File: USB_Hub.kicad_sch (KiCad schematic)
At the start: 44 parts, among them U4 VL822-QFN76, U5 AP7331-10WG-7, Y1 25MHz

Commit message: Updated schematics
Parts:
- added R24, R25, R26, R27: 100k, Resistor_SMD:R_0402_1005Metric, symbol Device:R
- C10, C11, C12, C13, C14, C16, C17, C27, C28, C29, C30, C31, C33, C34: value 100nF -> 0.1µF; LCSC C60474 -> C307331; Part_Number CC0402KRX7R7BB104 -> CL05B104KB54PNC
- C15, C19, C32: LCSC C77019 -> C15195; Part_Number GRM155R71H103KA88D -> CL05B103KB5NNNC
- C35: LCSC C59782 -> C15849; Part_Number CL10B105KO8NNNC -> CL10A105KB8NNNC
- C36: footprint (none) -> Capacitor_SMD:C_0603_1608Metric; LCSC C8032 -> C19666; Part_Number CL10A475KQ8NNNC -> CL10A475KO8NNNC
- C65, C66, C67, C68, C69, C70, C71, C72, C73, C74: footprint Capacitor_SMD:C_0201_0603Metric -> Capacitor_SMD:C_0402_1005Metric; LCSC C160831 -> C307331; Part_Number CL03A104KQ3NNNC -> CL05B104KB54PNC
- R17, R18, R19, R20: LCSC C105870 -> C25900; Part_Number RC0402JR-074K7L -> 0402WGF4701TCE
- R2, R22, R23, R7, R8: LCSC C60490 -> C25744; Part_Number RC0402FR-0710KL -> 0402WGF1002TCE
- R21: footprint Resistor_SMD:R_0603_1608Metric -> Resistor_SMD:R_0805_2012Metric_Pad1.20x1.40mm_HandSolder; LCSC C728611 -> C966572; Part_Number RT0603DRD0712K4L -> CQ05W8F1242T5E
- U4: footprint kicad_lceda:QFN-76_L9.0-W9.0-P0.40-EP6.3-TL -> VL822-QFN76:VL822-QFN76
- U5: footprint kicad_lceda:SOT-25_L3.0-W1.6-P0.95-LS2.8-BL -> AP7331-10WG-7:AP7331-10WG-7
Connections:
- net +3V3: now also R24.2, R25.2, R26.1, R27.1
- net SSTX3+: now reaches C69.2, U4.25 (SSTX3+)
- net SSTX4+: now reaches C71.2, U4.31 (SSTX4+)
- net SSTX2+: now reaches C67.2, U4.12 (SSTX2+)
- net SSTX2-: now reaches C68.2, U4.13 (SSTX2–)
- net USB_DFP0_EN: now reaches U4.2 (USBPE1)
- net USB_DFP0_EN: now also R24.1
- net USB_DFP2_EN: now reaches U4.21 (USBPE3)
- net USB_DFP2_EN: now also R26.2
- net SSTX3-: now reaches C70.2, U4.26 (SSTX3–)
- net SSTX1+: now reaches C65.2, U4.3 (SSTX1+)
- net SSTX4-: now reaches C72.2, U4.32 (SSTX4–)
- net USB_DFP3_EN: now reaches U4.39 (USBPE4)
- net USB_DFP3_EN: now also R27.2
- net SSTX1-: now reaches C66.2, U4.4 (SSTX1–)
- net SSTX0-: now reaches C74.1, U4.49 (SSTX0–)
- net SSTX0+: now reaches C73.1, U4.50 (SSTX0+)
- net USB_DFP1_EN: now reaches U4.76 (USBPE2)
- net USB_DFP1_EN: now also R25.1
- net USBOC1 renamed USB_DFP0_FLT
- net USBOC2 renamed USB_DFP1_FLT
- net USBOC3 renamed USB_DFP2_FLT
- net USBOC4 renamed USB_DFP3_FLT
- net USB_DFP0_DM renamed USB_DFP0_DN
- net USB_DFP1_DM renamed USB_DFP1_DN
- net USB_DFP2_DM renamed USB_DFP2_DN
- net USB_DFP3_DM renamed USB_DFP3_DN
- net USB_UFP_DM renamed USB_UFP_DN
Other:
- note added: "VBUS Enables"
- note added: "VBUS OC Input"
- note removed: "Disable USB Overcurrent Protection"
- moved on the sheet: R2, R22, R23, R7, R8

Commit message: Continue working on board layout
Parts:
- added R75: 4.7k, Resistor_SMD:R_0402_1005Metric, symbol Device:R
- added R76: 10k, Resistor_SMD:R_0402_1005Metric, symbol Device:R
- added R77: 2M, Resistor_SMD:R_0603_1608Metric, symbol Device:R
- Y1: symbol Device:Crystal -> Device:Crystal_GND24; LCSC C2962753 -> C9006; Part_Number XC32M4-25.000-F20LJDTL -> X322525MOB4SI
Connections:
- net GND: now also Y1.2, Y1.4, R76.2
- net VBUSDET: now also R77.2
- net XO: now also Y1.3; no longer Y1.2
- new net: R75.2, R76.1, R77.1
- new net +5V: R75.1
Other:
- note added: "VBUS Detect"

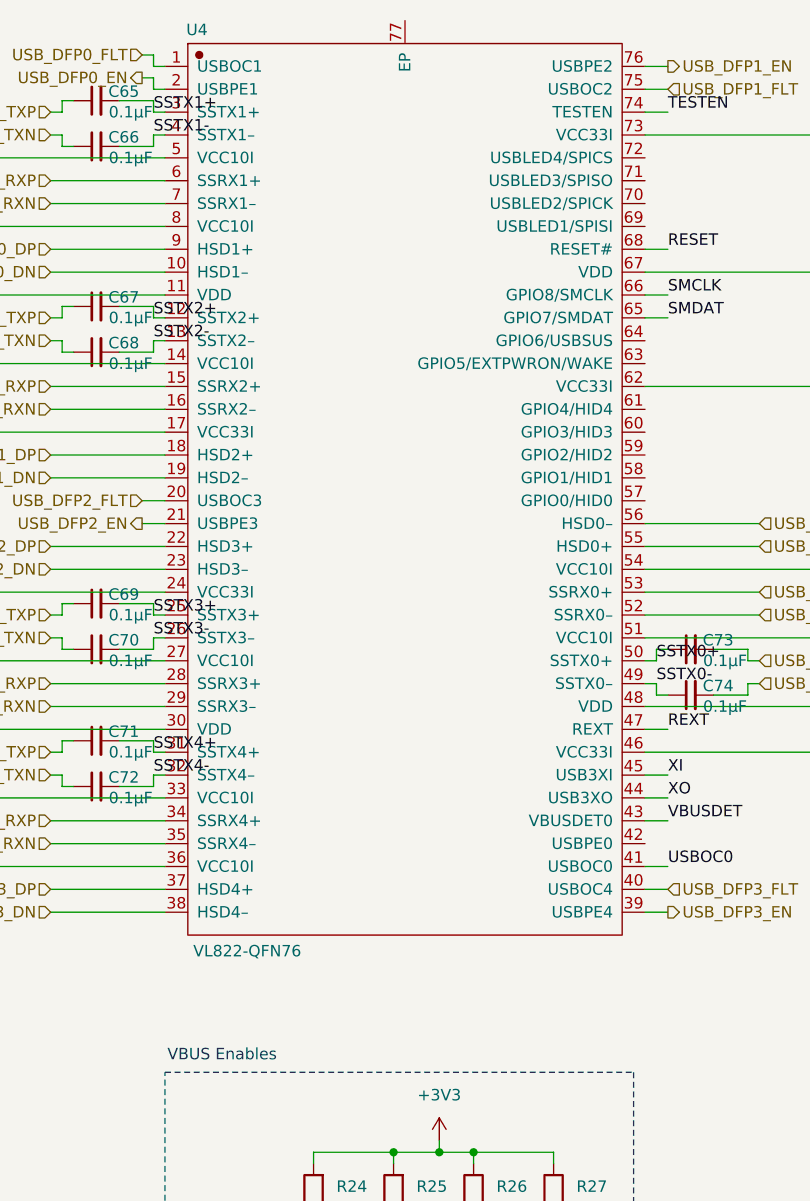
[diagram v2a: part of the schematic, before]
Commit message: Lay out more components
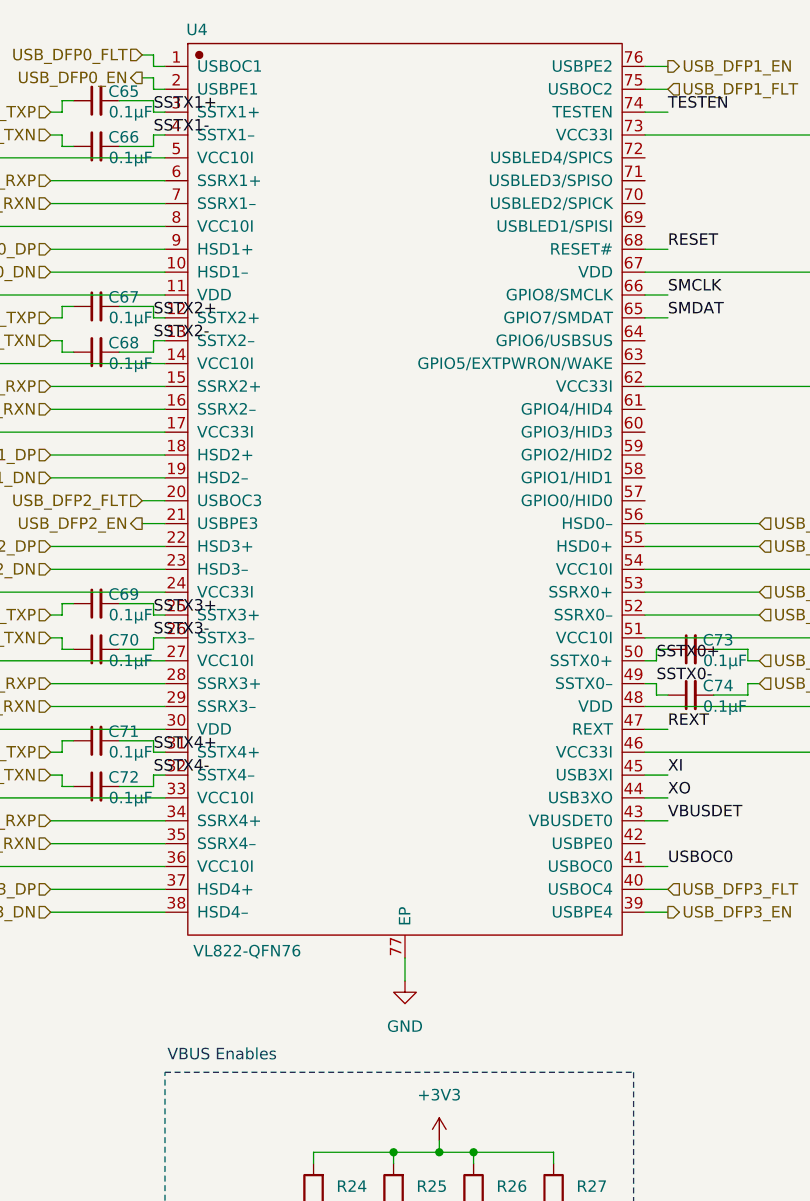
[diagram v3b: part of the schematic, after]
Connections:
- net GND: now also U4.77 (EP)
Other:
- moved on the sheet: U4
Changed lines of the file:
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@@
 	(wire
 		(pts
+			(xy 148.59 119.38) (xy 148.59 121.92)
+		)
+		(stroke
+			(width 0)
+			(type default)
+		)
+	)
+	(wire
+		(pts
 			(xy 20.32 110.49) (xy 20.32 115.57)
 		)
@@
 					(unit 1)
 				)
+			)
+		)
+	)
+	(symbol
+		(lib_id "power:GND")
+		(at 148.59 121.92 0)
+		(unit 1)
+		(exclude_from_sim no)
+		(in_bom yes)
+		(on_board yes)
+		(dnp no)
+		(fields_autoplaced yes)
+		(property "Reference" "#PWR0103"
+			(at 148.59 128.27 0)
+			(effects
+				(font
+					(size 1.27 1.27)
+				)
+				(hide yes)
+			)
+		)
+		(property "Value" "GND"
+			(at 148.59 127 0)
+			(effects
+				(font
+					(size 1.27 1.27)
+				)
+			)
+		)
+		(property "Footprint" ""
+			(at 148.59 121.92 0)
+			(effects
+				(font
+					(size 1.27 1.27)
+				)
+				(hide yes)
+			)
+		)
+		(property "Datasheet" ""
+			(at 148.59 121.92 0)
+			(effects
+				(font
+					(size 1.27 1.27)
+				)
+				(hide yes)
+			)
+		)
+		(property "Description" "Power symbol creates a global label with name \"GND\" , ground"
+			(at 148.59 121.92 0)
+			(effects
+				(font
+					(size 1.27 1.27)
+				)
+				(hide yes)
+			)
+		)
+		(pin "1"
+		)
+		(instances
+			(project "XG_Mobile_Dock"
+				(path "/f97e6956-ab08-42cb-8fed-03fa58e87f0e/ef21a87f-222f-4a81-a291-59975487be1d"
+					(reference "#PWR0103")
+					(unit 1)
+				)

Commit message: Updated board layout
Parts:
- C91, C92: LCSC C376770 -> C1653; Part_Number TCC0603COG180J500CT -> CL10C220JB8NNNC
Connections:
- net GND: now also U5.2 (GND)
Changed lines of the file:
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@@
 	)
 	(junction
+		(at 26.67 182.88)
+		(diameter 0)
+		(color 0 0 0 0)
+	)
+	(junction
 		(at 20.32 120.65)
 		(diameter 0)
@@
 	(wire
 		(pts
+			(xy 26.67 182.88) (xy 26.67 185.42)
+		)
+		(stroke
+			(width 0)
+			(type default)
+		)
+	)
+	(wire
+		(pts
 			(xy 245.11 93.98) (xy 245.11 102.87)
 		)
@@
 	(wire
 		(pts
+			(xy 35.56 182.88) (xy 26.67 182.88)
+		)
+		(stroke
+			(width 0)
+			(type default)
+		)
+	)
+	(wire
+		(pts
 			(xy 74.93 78.74) (xy 121.92 78.74)
 		)
@@
 	(wire
 		(pts
-			(xy 26.67 181.61) (xy 26.67 185.42)
+			(xy 26.67 181.61) (xy 26.67 182.88)
 		)
 		(stroke
@@
 	(wire
 		(pts
+			(xy 38.1 177.8) (xy 35.56 177.8)
+		)
+		(stroke
+			(width 0)
+			(type default)
+		)
+	)
+	(wire
+		(pts
 			(xy 20.32 120.65) (xy 64.77 120.65)
 		)
@@
 	(wire
 		(pts
+			(xy 35.56 177.8) (xy 35.56 182.88)
+		)
+		(stroke
+			(width 0)
+			(type default)
+		)
+	)
+	(wire
+		(pts
 			(xy 175.26 88.9) (xy 176.53 88.9)
 		)
@@
 			)
 		)
-		(property "LCSC" "C376770"
+		(property "LCSC" "C1653"
 			(at 256.54 123.19 0)
 			(effects
@@
 			)
 		)
-		(property "Part_Number" "TCC0603COG180J500CT"
+		(property "Part_Number" "CL10C220JB8NNNC"
 			(at 256.54 123.19 0)
 			(effects
@@
 			)
 		)
-		(property "LCSC" "C376770"
+		(property "LCSC" "C1653"
 			(at 266.7 123.19 0)
 			(effects
@@
 			)
 		)
-		(property "Part_Number" "TCC0603COG180J500CT"
+		(property "Part_Number" "CL10C220JB8NNNC"
 			(at 266.7 123.19 0)
 			(effects

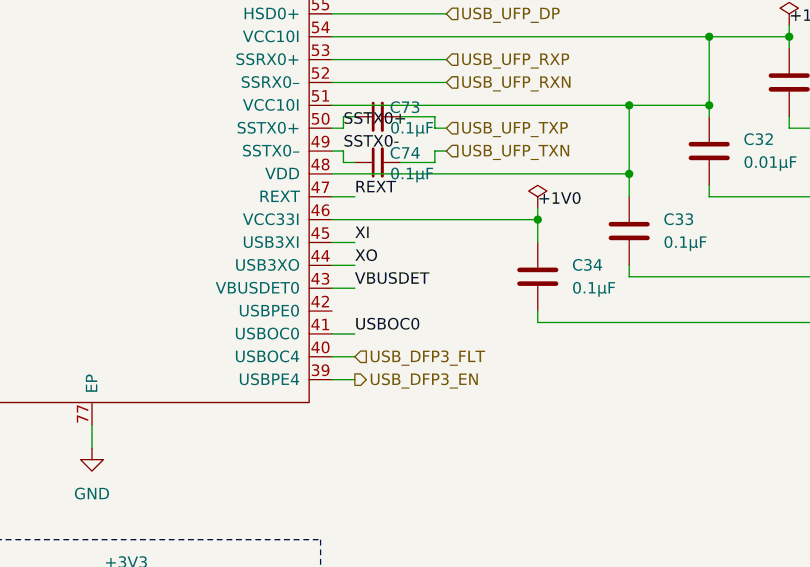
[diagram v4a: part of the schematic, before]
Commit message: Add TPS65987D charger circuit
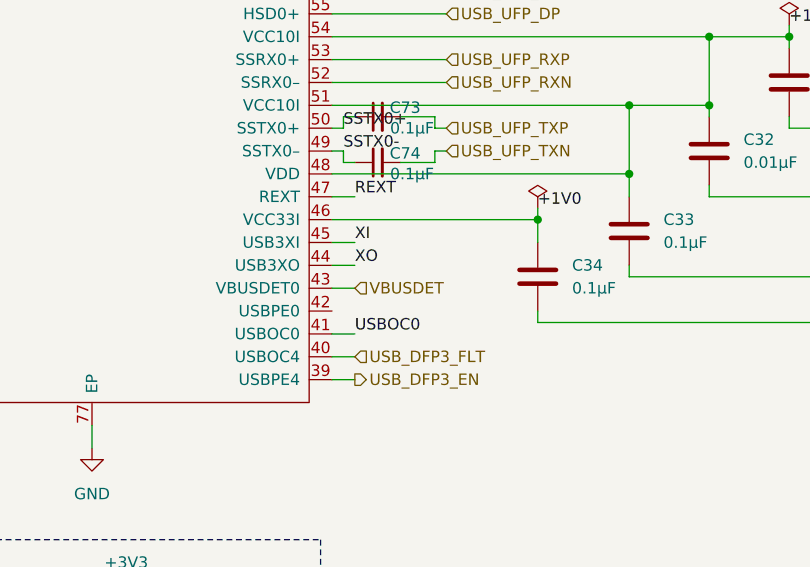
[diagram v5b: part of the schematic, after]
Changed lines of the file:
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@@
-		)
-	)
-	(label "VBUSDET"
-		(at 177.8 104.14 0)
-		(fields_autoplaced yes)
-		(effects
-			(font
-				(size 1.27 1.27)
-			)
-			(justify left bottom)
 		)
 	)
@@
 		)
 	)
+	(hierarchical_label "VBUSDET"
+		(shape input)
+		(at 177.8 104.14 0)
+		(fields_autoplaced yes)
+		(effects
+			(font
+				(size 1.27 1.27)
+			)
+			(justify left)
+		)
+	)

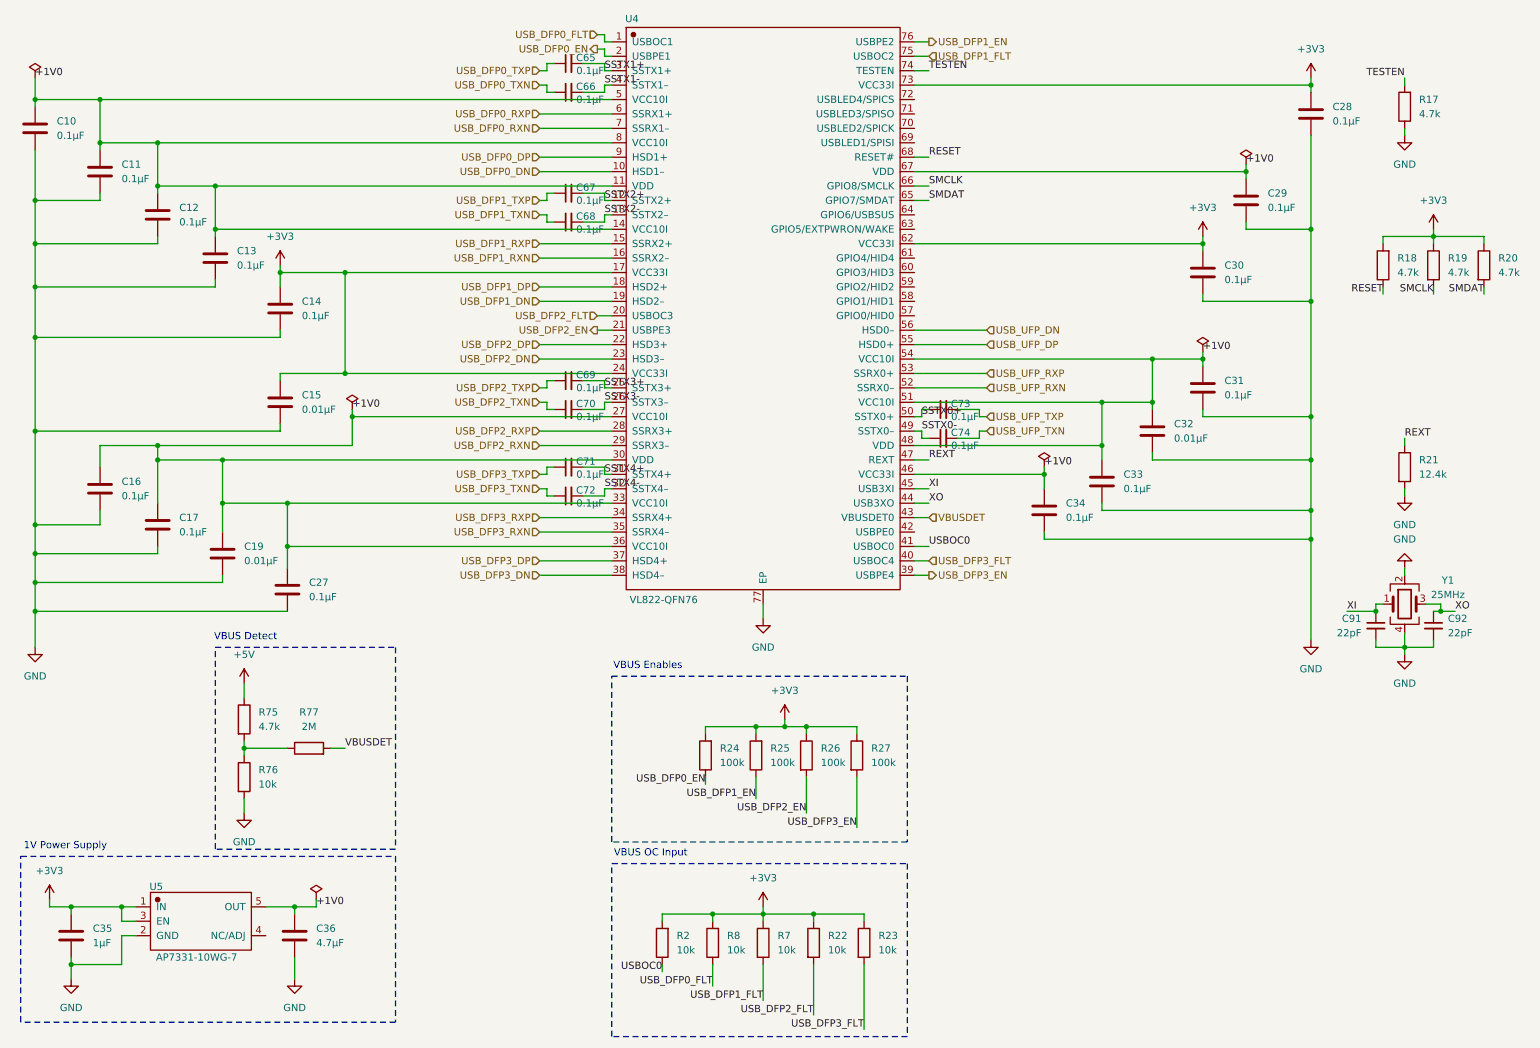
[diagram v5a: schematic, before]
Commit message: Added MCU
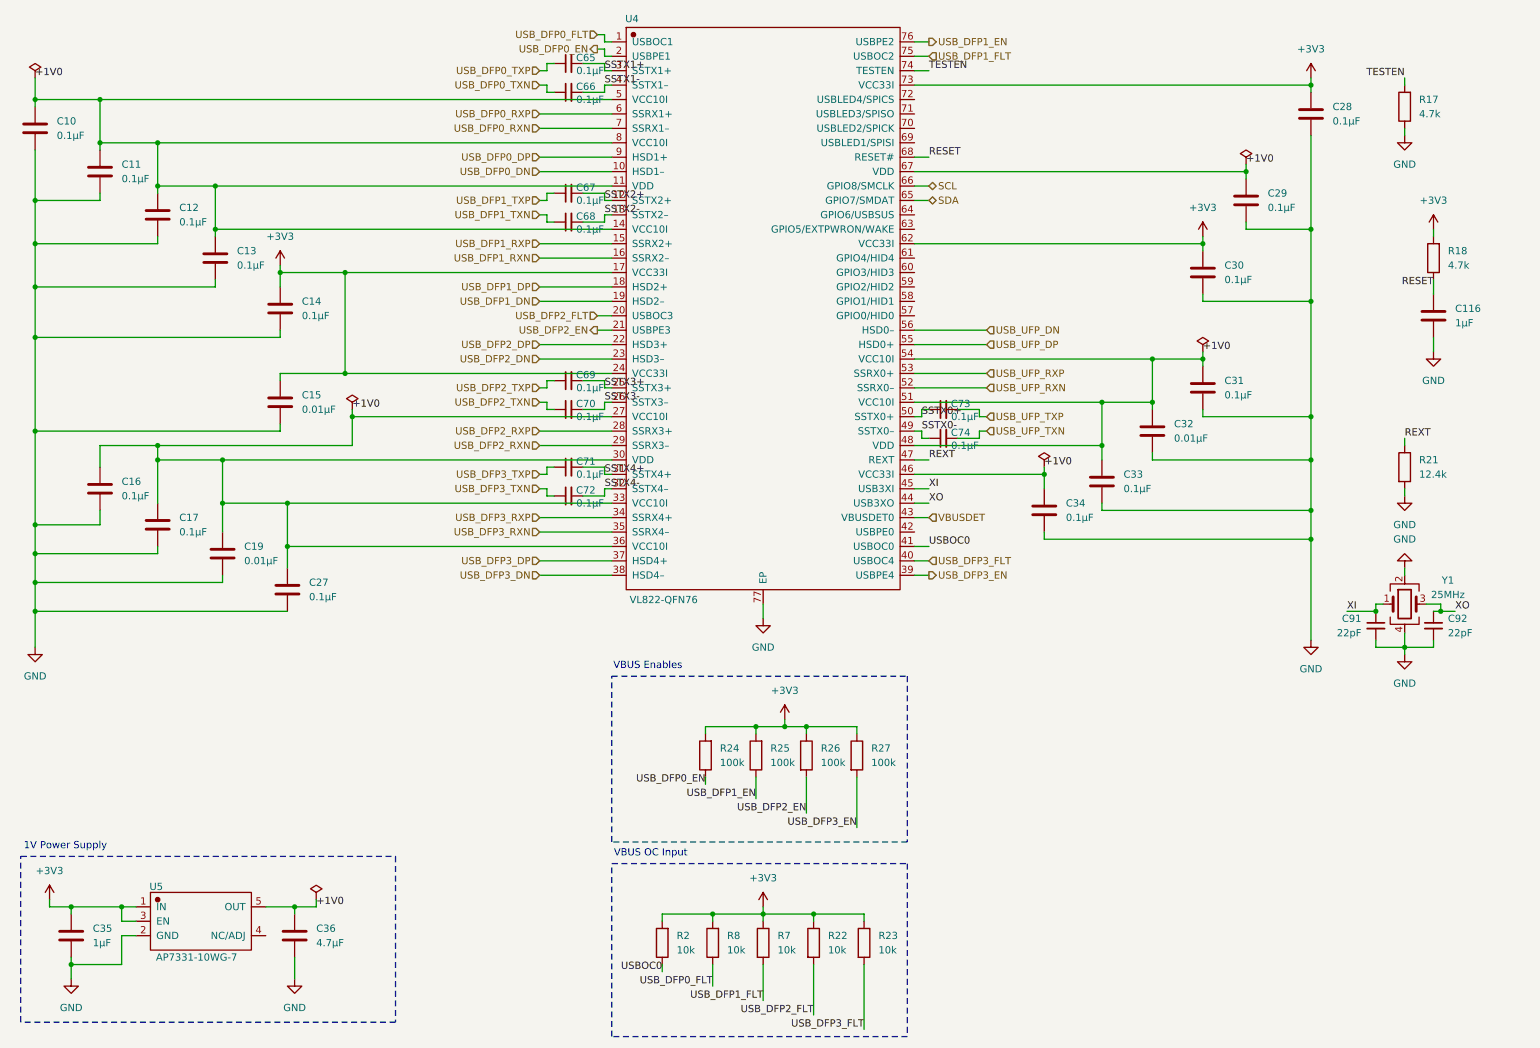
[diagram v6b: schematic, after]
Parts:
- removed R19, R20, R75: 4.7k, Resistor_SMD:R_0402_1005Metric, symbol Device:R
- removed R76: 10k, Resistor_SMD:R_0402_1005Metric, symbol Device:R
- removed R77: 2M, Resistor_SMD:R_0603_1608Metric, symbol Device:R
- added C116: 1µF, Capacitor_SMD:C_0402_1005Metric, symbol Device:C
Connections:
- net GND: now also C116.2
- net RESET: now also C116.1
- net SMCLK renamed SCL
- net SMDAT renamed SDA
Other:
- note removed: "VBUS Detect"
- moved on the sheet: R18
